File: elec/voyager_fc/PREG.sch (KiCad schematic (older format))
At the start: 34 parts

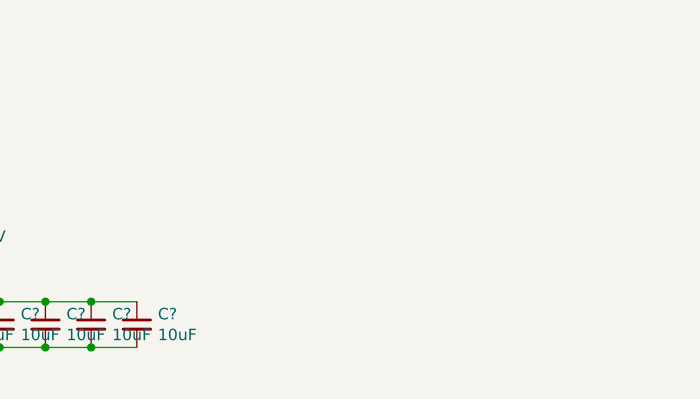
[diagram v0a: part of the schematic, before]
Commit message: Move connectors inside schematics
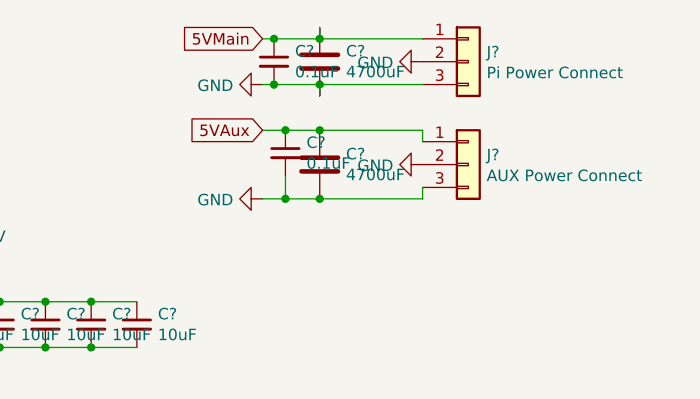
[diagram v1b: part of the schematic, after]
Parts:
- added C? (x2): 0.1uF, Capacitor_SMD:C_0603_1608Metric, symbol Device:C_Small
- added C? (x2): 4700uF, Capacitor_THT:CP_Radial_D10.0mm_P5.00mm, symbol Device:C
- added J?: AUX Power Connect, Connector_PinHeader_2.54mm:PinHeader_1x03_P2.54mm_Vertical, symbol Connector_Generic:Conn_01x03
- added J?: Pi Power Connect, Connector_PinHeader_2.54mm:PinHeader_1x03_P2.54mm_Vertical, symbol Connector_Generic:Conn_01x03
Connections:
- net 5VAux: now also C?.1, C?.1, J?.1 (Pin_1)
- net 5VMain: now also C?.1, C?.1, J?.1 (Pin_1)
- net GND: now also C?.2, C?.2, C?.2, C?.2, J?.2 (Pin_2), J?.2 (Pin_2), J?.3 (Pin_3), J?.3 (Pin_3)

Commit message: Place all components and start route
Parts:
- removed U?: TPS2121RUXR, IC_TPS2121RUXR, symbol TPS2121RUXR:TPS2121RUXR
- added U4: TPS2121RUXR, IC_TPS2121RUXR, symbol TPS2121RUXR:TPS2121RUXR
- C10, C11, C12, C13, C14, C15, C16, C17, C18, C23, C24, C26, C27, C28, C29, C7, C8, C9: renamed from C?; footprint Capacitor_SMD:C_0805_2012Metric -> Capacitor_SMD:C_0603_1608Metric
- C19, C20, C22, C30, C31: renamed from C?; footprint Capacitor_SMD:C_0603_1608Metric -> Capacitor_SMD:C_0402_1005Metric
- gave numbers to parts that had none: 16
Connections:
- net +3V3: now also U4.3 (CP2)
- net +5V: no longer C23.1, C24.1, C26.1, C27.1, C28.1, C29.1
- net 5VAux: now also U4.2 (IN2)
- net 5VMain: now also U4.7 (IN1)
- net GND: now also U4.12 (GND)
- net PMUX_OV1: now also U4.5 (OV1)
- net PMUX_OV2: now also U4.4 (OV2)
- net PMUX_PR1: now also U4.6 (PR1)
- net PMUX_ST: now also U4.9 (ST)
- net at R45.1: now also U4.10 (ILIM)
- net at C20.1: now also U4.11 (SS)
- new net 5V: C23.1, C24.1, C26.1, C27.1, C28.1, C29.1, U4.1 (OUT), U4.8 (OUT)
